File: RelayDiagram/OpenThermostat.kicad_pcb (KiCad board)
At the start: 2 copper layers, 162.6 x 102.4 mm, 95 parts, among them J1 Conn_01x08_Female, J2 Conn_01x15_Female, J3 Conn_01x15_Female, J4 Conn_01x09_Female, Q1 Q_NMOS_DGS, Q10 Q_NMOS_DGS, Q11 Q_NMOS_DGS, Q12 Q_NMOS_DGS, Q2 Q_NMOS_DGS, Q3 Q_NMOS_DGS, Q4 Q_NMOS_DGS, Q5 Q_NMOS_DGS, Q6 Q_NMOS_DGS, Q7 Q_NMOS_DGS, Q8 Q_NMOS_DGS, Q9 Q_NMOS_DGS, SW2 SW_Push, SW3 SW_Push, SW4 SW_Push, SW5 SW_Push, SW6 SW_Push, U1 PCF8574, U10 MB10S-13, U11 L7805CV, U2 LCD, U3 DHT11, U4 EE2-3TNU-L_DPDT_Relay, U5 EE2-3TNU-L_DPDT_Relay, U6 EE2-3TNU-L_DPDT_Relay, U7 EE2-3TNU-L_DPDT_Relay, U8 EE2-3TNU-L_DPDT_Relay, U9 EE2-3TNU-L_DPDT_Relay

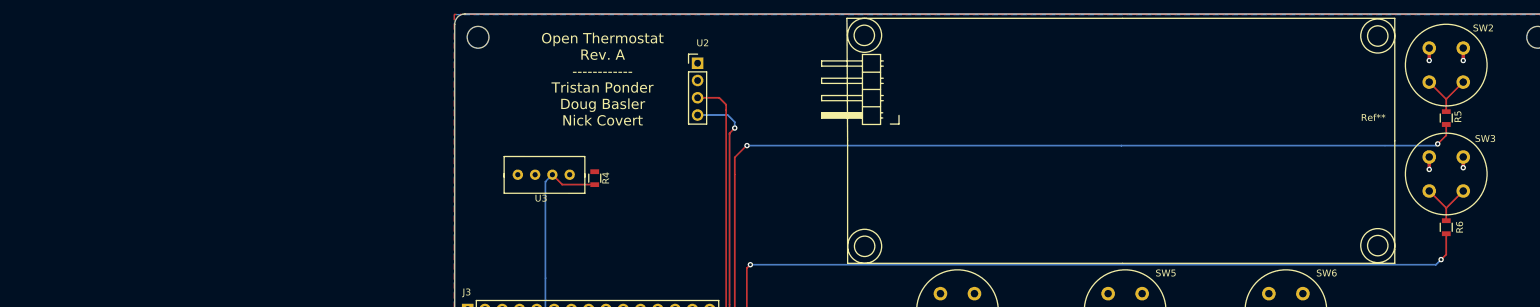
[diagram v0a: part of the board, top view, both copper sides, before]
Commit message: added mounting holes and power indicator LED
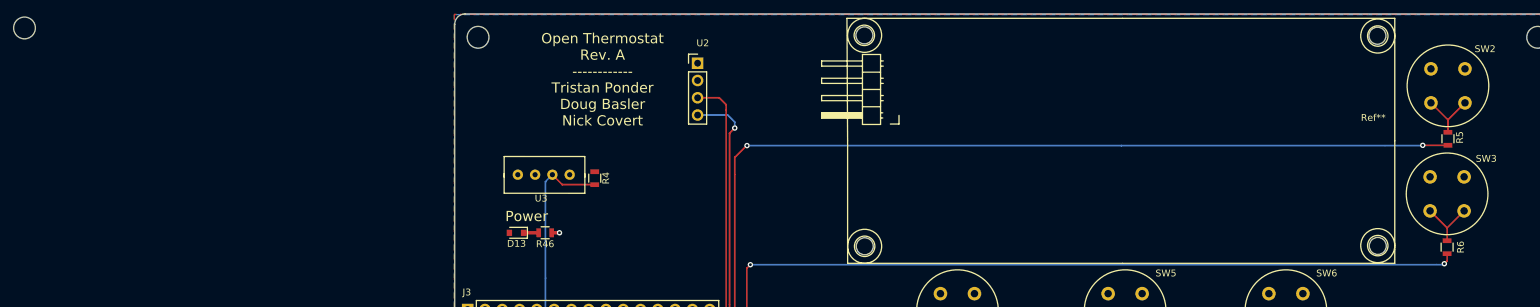
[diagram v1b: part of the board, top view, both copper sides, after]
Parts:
- added ?: MountingHole_2.5mm, Mounting_Holes:MountingHole_2.5mm, F.Cu at (186.6, 60.6)
- added ?: MountingHole_2.5mm, Mounting_Holes:MountingHole_2.5mm, F.Cu at (186.7, 91.5)
- added ?: MountingHole_2.5mm, Mounting_Holes:MountingHole_2.5mm, F.Cu at (111.3, 91.5)
- added ?: , solarcar-misc:MountingHole_3.2mm_M3, F.Cu at (-12.2, 59.5)
- added ?: MountingHole_2.5mm, Mounting_Holes:MountingHole_2.5mm, F.Cu at (111.3, 60.6)
- added D13: LED, Diodes_SMD:D_0805, F.Cu at (60.1, 89.6)
- added R46: 100, Resistors_SMD:R_0805, F.Cu at (64.3, 89.6)
- moved R5 3.06 mm to (197.0, 75.7)
- moved SW2 3.06 mm to (194.5, 70.5)
- moved R6 2.92 mm to (196.9, 91.7)
- moved SW3 2.92 mm to (194.4, 86.3)
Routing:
- net GND: track 53.4 -> 47.4 mm, vias 22 -> 19
- net Net-(J2-Pad9): track 154.8 -> 152.6 mm
- net Net-(D13-Pad1): track 0.00 -> 2.21 mm
- net Net-(J2-Pad8): track 173.3 -> 171.3 mm
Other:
- board text added: "Power"

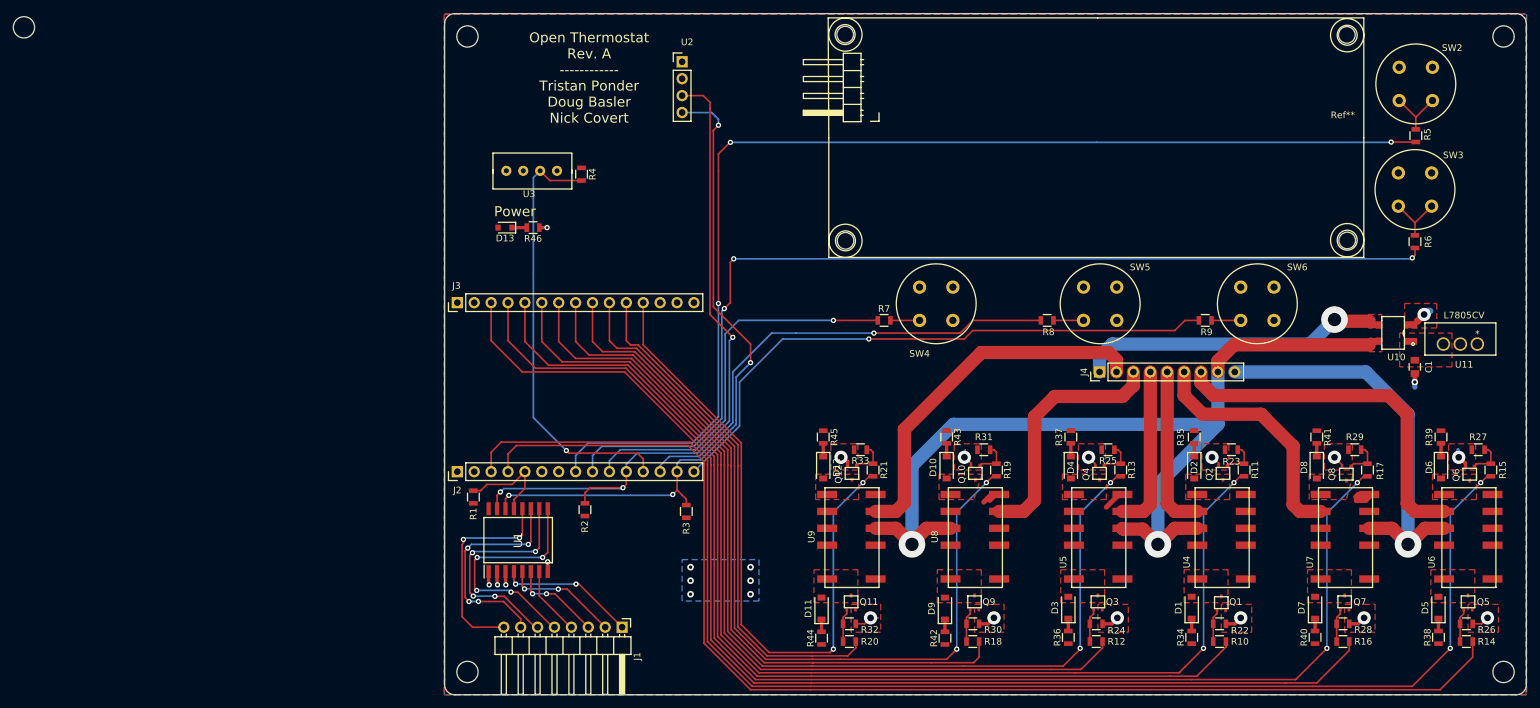
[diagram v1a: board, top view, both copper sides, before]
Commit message: Changed to big boy header and added great logo
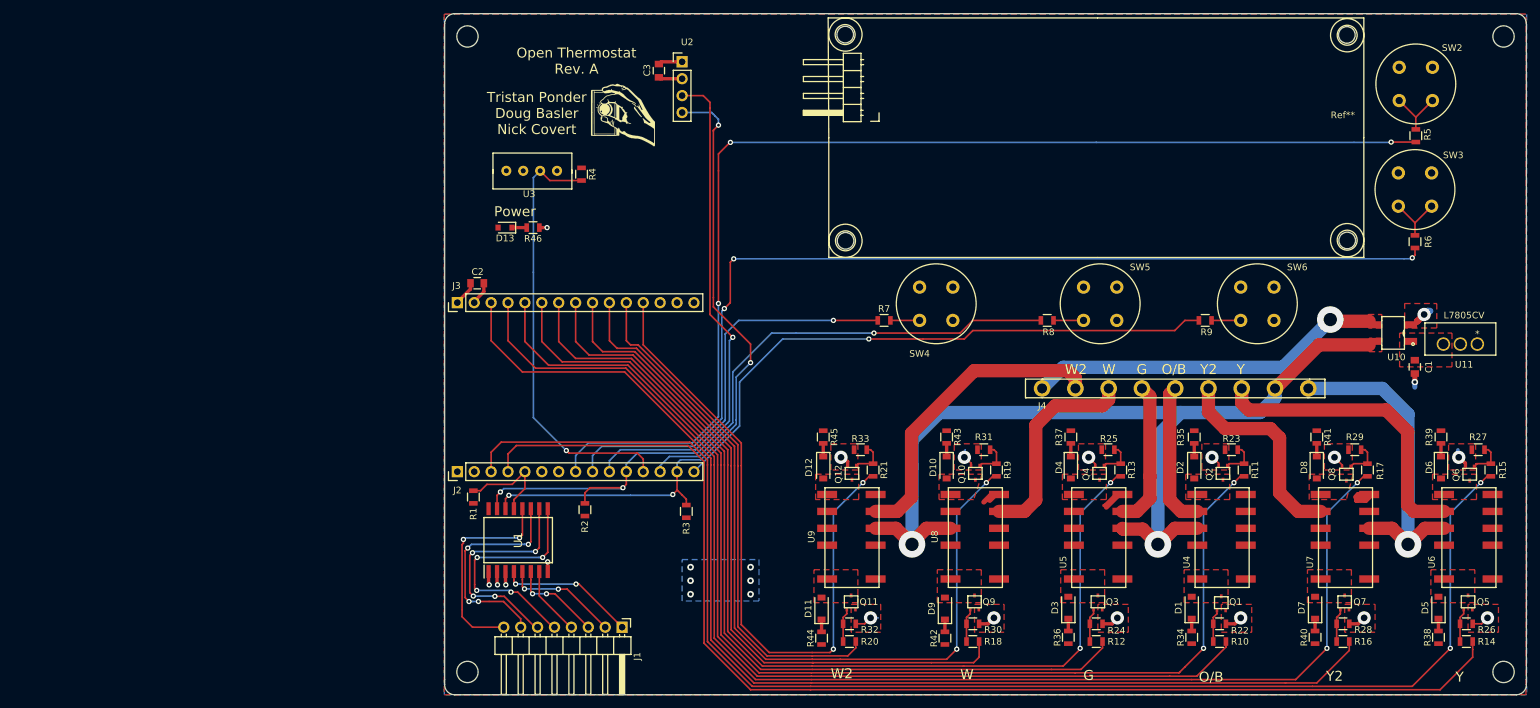
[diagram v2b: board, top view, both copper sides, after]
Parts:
- removed the ? at (-12.2, 59.5)
- added C2: 10uF, solarcar-device:Capacitor_0805, F.Cu at (55.9, 97.9)
- added C3: 10uF, solarcar-device:Capacitor_0805, F.Cu at (83.2, 66.0)
- added G***: LOGO, SeniorDesign:Great_Logo, F.Cu at (77.9, 72.6)
- J4: footprint Pin_Headers:Pin_Header_Straight_1x09_Pitch2.54mm -> SeniorDesign:5mmPtichBlockHeader
- moved J4 8.98 mm to (140.8, 113.7), turned to 0 degrees
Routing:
- net /RC: track 61.5 -> 49.4 mm
- net +5V: track 14.7 -> 25.5 mm
- net Net-(J4-Pad1): track 45.2 -> 55.0 mm
- net Net-(J4-Pad2): track 54.8 -> 46.4 mm
- net Net-(J4-Pad7): track 54.1 -> 45.8 mm
- net GND: track 47.4 -> 54.6 mm
- net Net-(J4-Pad3): track 37.4 -> 31.7 mm
- net Net-(J4-Pad6): track 36.4 -> 31.4 mm
- net /R: track 142.0 -> 139.1 mm
- net Net-(J4-Pad5): track 24.8 -> 22.0 mm
- net Net-(J4-Pad4): track 24.6 -> 21.9 mm
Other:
- board text added: "G"
- board text added: "O/B"
- board text added: "Open Thermostat Rev. A"
- board text added: "Tristan Ponder Doug Basler Nick Covert"
- board text added: "W"
- board text added: "W2"
- board text added: "Y"
- board text added: "Y2"
- board text removed: "Open Thermostat Rev. A ------------ Tristan Ponder Doug Basler Nick Covert"

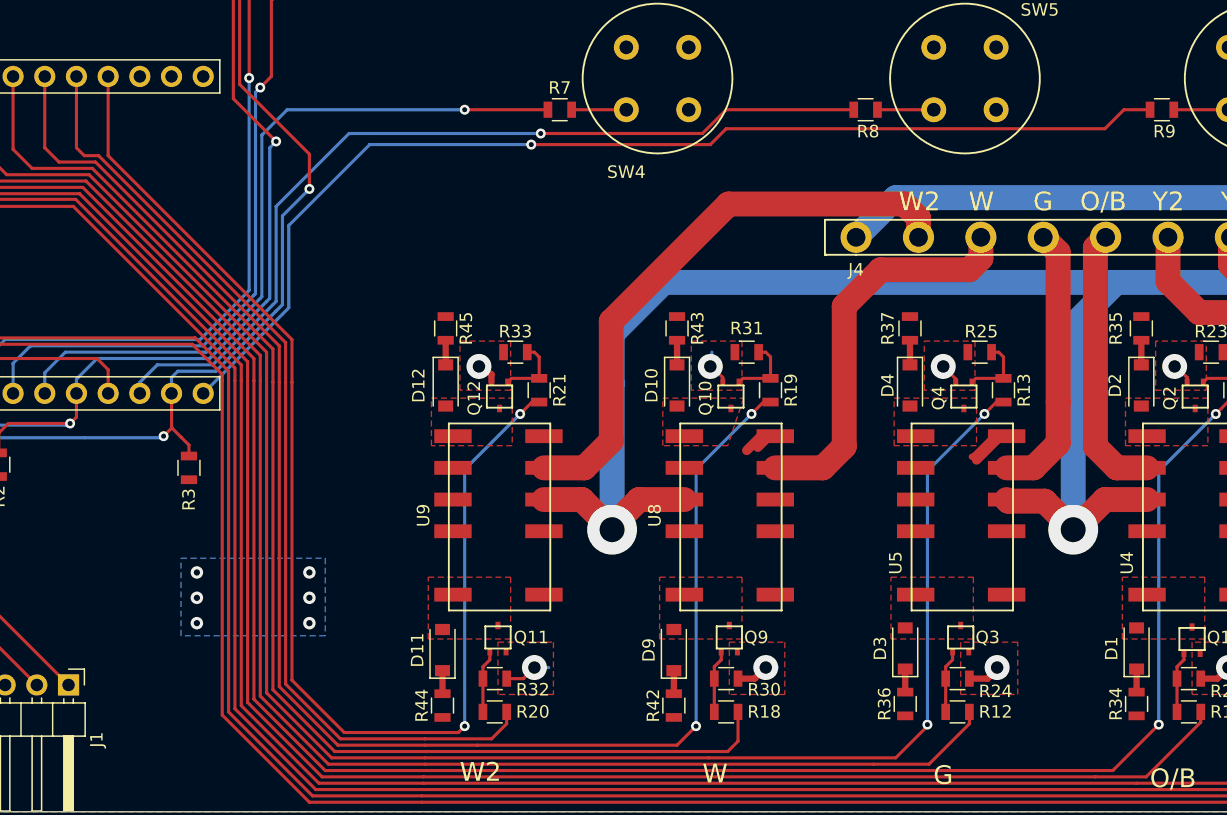
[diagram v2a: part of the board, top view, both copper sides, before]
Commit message: changed ports on micro controller to get input only ports connected to switches
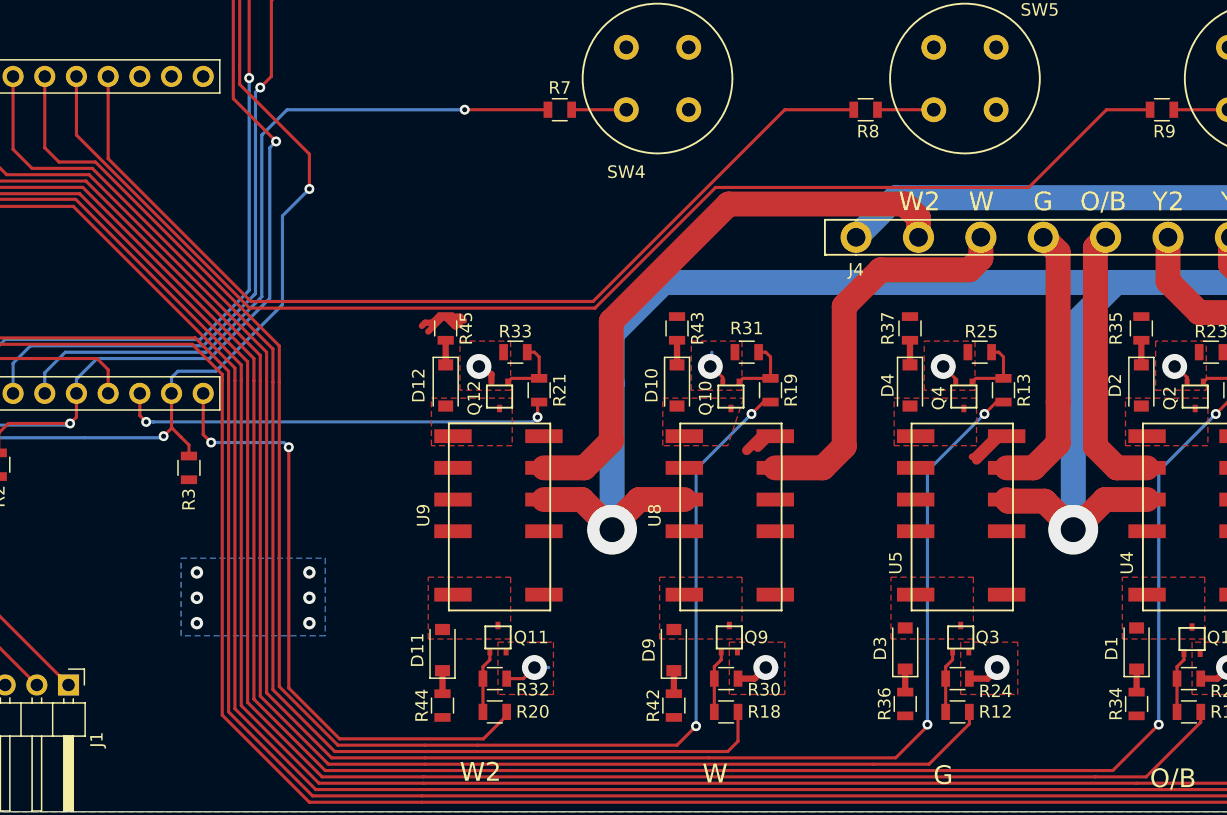
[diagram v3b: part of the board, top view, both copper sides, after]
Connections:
- R20 pad 2: Net-(J3-Pad11) -> Net-(J2-Pad15)
- R21 pad 2: Net-(J3-Pad12) -> Net-(J2-Pad13)
- R8 pad 1: Net-(J2-Pad13) -> Net-(J3-Pad12)
- R9 pad 1: Net-(J2-Pad15) -> Net-(J3-Pad11)
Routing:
- net Net-(J2-Pad15): track 89.2 -> 50.1 mm, vias 1 -> 2
- net Net-(J2-Pad13): track 71.6 -> 35.3 mm, vias 1 -> 2
- net Net-(J3-Pad11): track 77.3 -> 103.1 mm
- net Net-(J3-Pad12): track 99.1 -> 77.5 mm, vias 2 -> 0
- net +5V: track 25.5 -> 33.8 mm

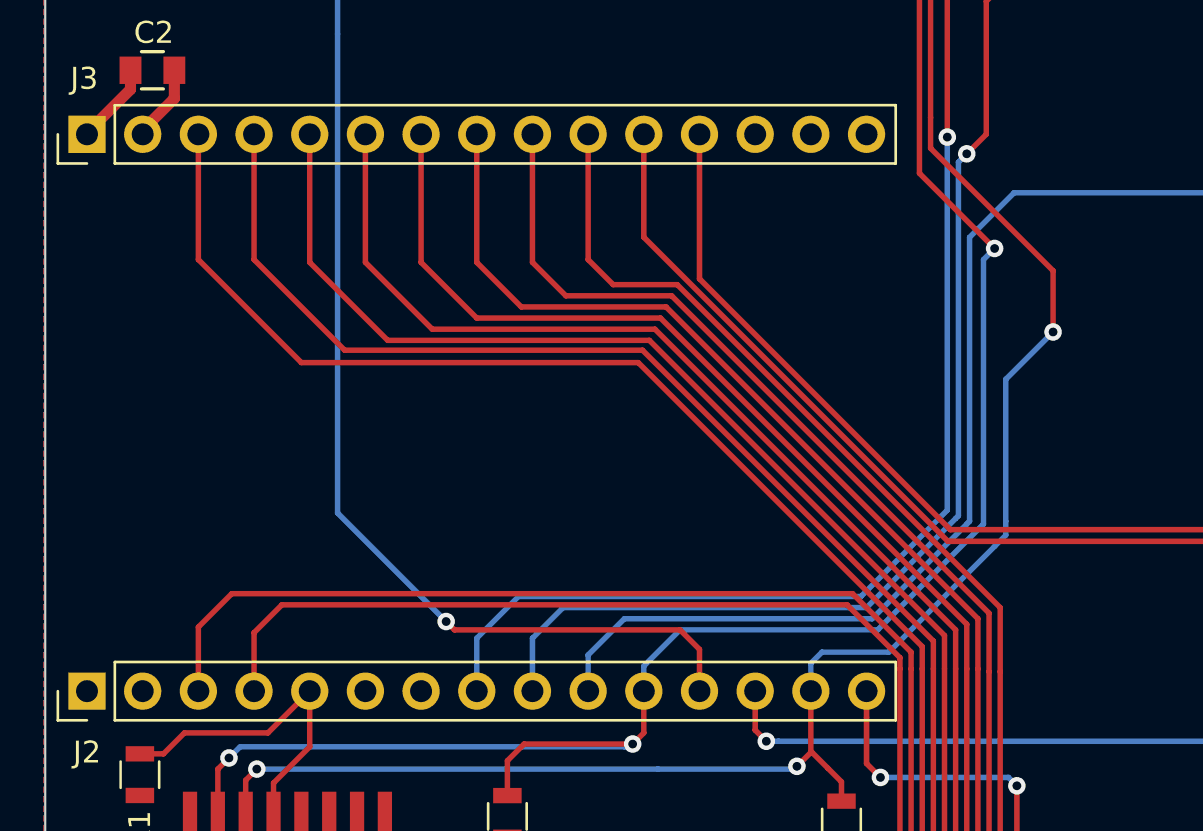
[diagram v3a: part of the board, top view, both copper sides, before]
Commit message: Added pull up resistors
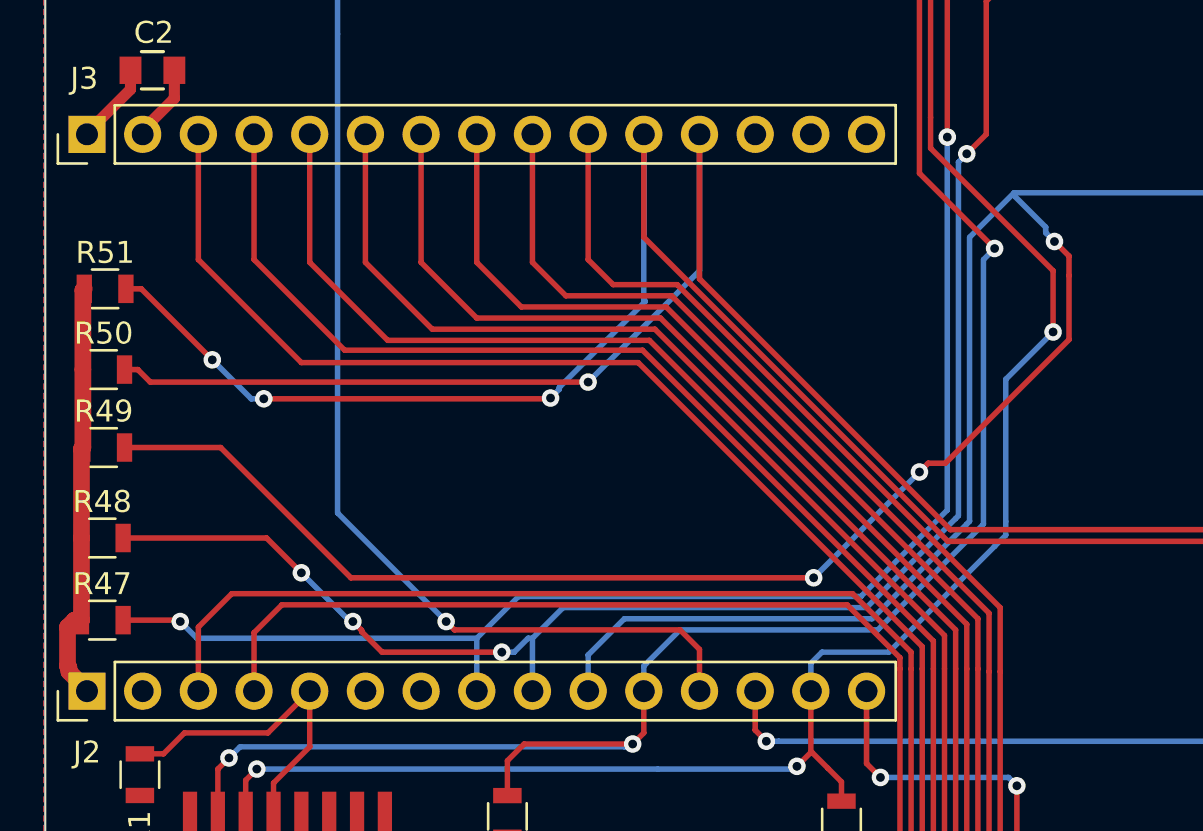
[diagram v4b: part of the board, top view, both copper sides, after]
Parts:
- added R47: 10K, Resistors_SMD:R_0805, F.Cu at (53.7, 123.0)
- added R48: 10K, Resistors_SMD:R_0805, F.Cu at (53.7, 119.3)
- added R49: 10K, Resistors_SMD:R_0805, F.Cu at (53.7, 115.1)
- added R50: 10K, Resistors_SMD:R_0805, F.Cu at (53.7, 111.6)
- added R51: 10K, Resistors_SMD:R_0805, F.Cu at (53.8, 107.9)
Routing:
- net Net-(J2-Pad10): track 58.3 -> 116.1 mm, vias 1 -> 4
- net Net-(J3-Pad11): track 103.1 -> 138.4 mm, vias 0 -> 3
- net Net-(J3-Pad12): track 77.5 -> 112.2 mm, vias 0 -> 1
- net Net-(J2-Pad9): track 152.6 -> 173.7 mm, vias 3 -> 6
- net Net-(J2-Pad1): track 0.00 -> 19.2 mm
- net Net-(J2-Pad8): track 171.3 -> 187.8 mm, vias 3 -> 4
